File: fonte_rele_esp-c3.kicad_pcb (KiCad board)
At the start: 2 copper layers, 67.5 x 55 mm, 34 parts, among them J1 Screw_Terminal_01x02, J2 Conn_01x05_Pin, J3 Screw_Terminal_01x03, K1 G5LE-1, Q1 AO3400A, U1 AZ1117CH2-3.3, U2 HS-40012, U3 ESP32-C3-WROOM-02

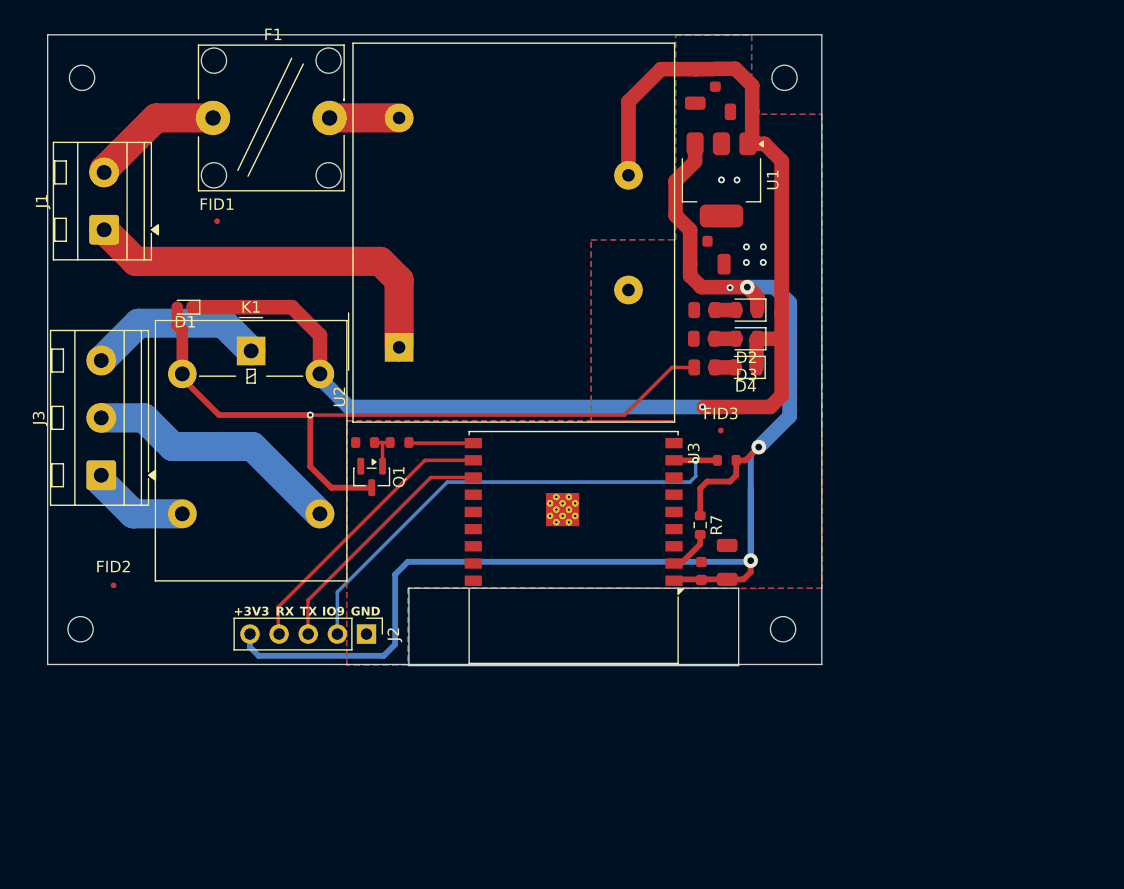
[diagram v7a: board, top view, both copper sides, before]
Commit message: Adiciona gerbers, atualiza PCB e documenta jumper externo do COM do rele
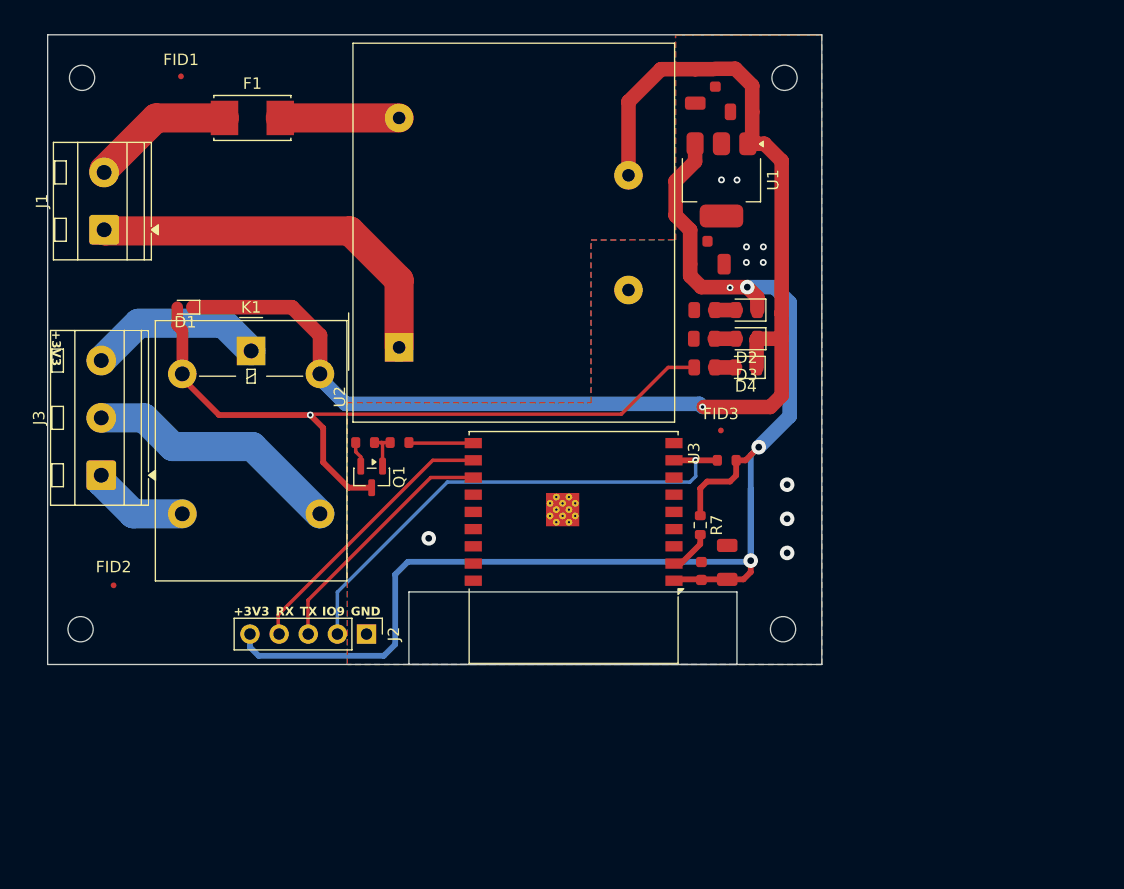
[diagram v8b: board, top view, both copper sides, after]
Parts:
- F1: footprint Fuse:Fuseholder_Cylinder-5x20mm_Bulgin_FX0456_Vertical_Closed -> Fuse:Fuseholder_Littelfuse_Nano2_157x
- moved FID1 13.0 mm to (117.1, 86.9)
- moved F1 3.43 mm to (123.3, 90.5)
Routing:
- net AC: track 6.06 -> 10.4 mm
- net GND: track 0.00 -> 2.24 mm, vias 6 -> 10
- net Net-(J1-Pin_2): track 11.6 -> 12.6 mm
- net /DRAIN: track 64.3 -> 63.4 mm
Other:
- board size 67.5 x 55 mm -> 67.5 x 54.9 mm
